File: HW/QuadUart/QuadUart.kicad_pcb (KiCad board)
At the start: 2 copper layers, 80.3 x 48.7 mm, 93 parts, among them J1 USB_C_Receptacle_USB2.0, J2 Conn_02x05_Odd_Even, J3 Conn_02x10_Odd_Even, Q1 BC847, Q2 BC847, SW1 SW_DIP_x04, SW2 SW_DIP_x01, SW3 SW_DIP_x01, U1 LN1134-3.3V, U10 SN74LV4T125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

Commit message: Finished layout, added Gerbers
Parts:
- removed C7, C8: 27pF, Capacitor_SMD:C_0603_1608Metric_Pad1.08x0.95mm_HandSolder
- added D11: LED, LED_SMD:LED_0603_1608Metric_Pad1.05x0.95mm_HandSolder, F.Cu at (170.7, 84.2)
- added J4: Conn_01x05, Connector_PinHeader_2.54mm:PinHeader_1x05_P2.54mm_Vertical, F.Cu at (192.9, 63.0)
- added LOGO1: Logo_Open_Hardware_Small, Symbol:OSHW-Logo_7.5x8mm_SilkScreen, F.Cu at (188.3, 70.2)
- added MARK1: LOGO, Kicad_Library:FOX_LOGO_MASK, B.Cu at (185.7, 86.6)
- added MARK2: LOGO, Kicad_Library:FOX_LOGO_SILK, F.Cu at (185.7, 86.6)
- added R31: 0R, Resistor_SMD:R_0603_1608Metric_Pad0.98x0.95mm_HandSolder, F.Cu at (169.2, 77.8)
- added R32: R, Resistor_SMD:R_0603_1608Metric_Pad0.98x0.95mm_HandSolder, F.Cu at (167.3, 84.2)
- Y1: value Crystal_GND24 -> Crystal_GND2; footprint Crystal:Crystal_SMD_3225-4Pin_3.2x2.5mm -> Crystal:Resonator_SMD_muRata_CSTxExxV-3Pin_3.0x1.1mm
- moved R2 10.6 mm to (158.5, 69.0), turned to 90 degrees
- moved C13 8.60 mm to (166.3, 53.1), turned to 270 degrees
- moved R24 7.23 mm to (164.8, 53.1), turned to 270 degrees
- moved R4 2.98 mm to (167.8, 87.0), turned to 180 degrees
- moved R1 2.72 mm to (158.5, 79.8), turned to 270 degrees
- moved FB2 2.46 mm to (161.2, 64.4), turned to 180 degrees
- moved C18 1.35 mm to (168.1, 73.0), turned to 180 degrees
- moved R27 1.34 mm to (205.1, 80.8), turned to 270 degrees
- moved R29 1.27 mm to (206.9, 67.9), turned to 90 degrees
- moved R3 1.26 mm to (164.0, 87.0), turned to 0 degrees
- moved R30 1.15 mm to (205.1, 67.9), turned to 90 degrees
- moved R28 1.10 mm to (206.9, 80.8), turned to 270 degrees
- moved R19 1.04 mm to (167.9, 53.1), turned to 270 degrees
- moved FB1 0.97 mm to (161.2, 66.3)
- moved R20 0.64 mm to (166.9, 63.1)
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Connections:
- C15 pad 1: VCC -> +3V3
- C17 pad 1: +3V3 -> VCC
- R14 pad 2: VCC -> /PWR_1
- R16 pad 2: VDD -> /PWR_2
- SW2 pad 1: Net-(C11-Pad1) -> VDD
- SW2 pad 2: VDD -> Net-(C11-Pad1)
- SW3 pad 1: Net-(C11-Pad1) -> VCC
- SW3 pad 2: VCC -> Net-(C11-Pad1)
- U10 pad 11: /DTR_2_UC -> /RX_3_RES
- U10 pad 12: /DTR_2_RES -> /RX_3_UC
- U10 pad 14: VCC -> +3V3
- U10 pad 2: /TX_1_UC -> /RX_2_RES
- U10 pad 3: /TX_1_RES -> /RX_2_UC
- U10 pad 5: /TX_2_UC -> /RX_1_RES
- U10 pad 6: /TX_2_RES -> /RX_1_UC
- U10 pad 8: /DTR_1_RES -> /RX_4_UC
- U10 pad 9: /DTR_1_UC -> /RX_4_RES
- U11 pad 2: /TX_3_UC -> /TX_4_UC
- U11 pad 3: /TX_3_RES -> /TX_4_RES
- U11 pad 5: /TX_4_UC -> /TX_3_UC
- U11 pad 6: /TX_4_RES -> /TX_3_RES
- U2 pad 1: /TX_2_RES -> /RX_2_RES
- U2 pad 3: /TX_1_RES -> /RX_1_RES
- U2 pad 4: /RX_2_RES -> /TX_2_RES
- U2 pad 6: /RX_1_RES -> /TX_1_RES
- U3 pad 1: /TX_4_RES -> Net-(U3-Pad1)
- U3 pad 3: /TX_3_RES -> Net-(U3-Pad3)
- U3 pad 4: /RX_4_RES -> /TX_4_RES
- U3 pad 6: /RX_3_RES -> /TX_3_RES
- U4 pad 1: /D- -> /D+
- U4 pad 3: /D- -> Net-(U4-Pad3)
- U4 pad 4: /D+ -> Net-(U4-Pad4)
- U4 pad 6: /D+ -> /D-
- U6 pad 4: Net-(U6-Pad4) -> /RX_4_RES
- U6 pad 6: Net-(U6-Pad6) -> /RX_3_RES
- U7 pad 1: /LED_RX_3 -> /LED_TX_2
- U7 pad 11: Net-(U7-Pad11) -> /DTR_3_UC
- U7 pad 12: Net-(U7-Pad12) -> /DTR_4_UC
- U7 pad 13: Net-(U7-Pad13) -> /LED_TX_3
- U7 pad 14: Net-(U7-Pad14) -> /LED_RX_3
- U7 pad 15: Net-(U7-Pad15) -> /LED_TX_4
- U7 pad 16: Net-(U7-Pad16) -> /LED_RX_4
- U7 pad 17: Net-(U7-Pad17) -> /PGEC2
- U7 pad 18: Net-(U7-Pad18) -> /PGED2
- U7 pad 2: /LED_TX_4 -> /LED_RX_1
- U7 pad 21: Net-(U7-Pad21) -> /RX_4_UC
- U7 pad 29: Net-(U7-Pad29) -> /TX_4_UC
- U7 pad 3: /LED_RX_4 -> /LED_TX_1
- U7 pad 31: /RX_2_UC -> /RX_3_UC
- U7 pad 32: /TX_2_UC -> /TX_3_UC
- U7 pad 4: /TX_DBG -> /TX_2_UC
- U7 pad 43: /RX_4_UC -> Net-(U7-Pad43)
- U7 pad 49: /TX_4_UC -> Net-(U7-Pad49)
- U7 pad 5: /RX_3_UC -> /RX_1_UC
- U7 pad 50: /RX_1_UC -> /RX_DBG
- U7 pad 51: /TX_1_UC -> /TX_DBG
- U7 pad 54: /DTR_3_UC -> Net-(U7-Pad54)
- U7 pad 55: /DTR_4_UC -> Net-(U7-Pad55)
- U7 pad 6: /TX_3_UC -> /TX_1_UC
- U7 pad 60: /LED_TX_1 -> Net-(U7-Pad60)
- U7 pad 61: /LED_RX_1 -> Net-(U7-Pad61)
- U7 pad 62: /LED_TX_2 -> Net-(U7-Pad62)
- U7 pad 63: /LED_RX_2 -> Net-(U7-Pad63)
- U7 pad 64: /LED_TX_3 -> /LED_RX_2
- U7 pad 8: /RX_DBG -> /RX_2_UC
- U9 pad 11: /RX_4_RES -> /DTR_1_UC
- U9 pad 12: /RX_4_UC -> /DTR_1_RES
- U9 pad 14: +3V3 -> VCC
- U9 pad 2: /RX_1_RES -> /TX_2_UC
- U9 pad 3: /RX_1_UC -> /TX_2_RES
- U9 pad 5: /RX_2_RES -> /TX_1_UC
- U9 pad 6: /RX_2_UC -> /TX_1_RES
- U9 pad 8: /RX_3_UC -> /DTR_2_RES
- U9 pad 9: /RX_3_RES -> /DTR_2_UC
- Y1 pad 3: /OSC2 -> Net-(R31-Pad1)
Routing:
- net +3V3: track 0.00 -> 175.5 mm, vias 0 -> 4
- net Net-(C11-Pad1): track 0.00 -> 121.7 mm, vias 0 -> 2
- net /~MCLR~: track 0.00 -> 60.3 mm, vias 0 -> 4
- net /PWR_2: track 0.00 -> 50.5 mm, vias 0 -> 6
- net /PWR_1: track 0.00 -> 43.4 mm, vias 0 -> 2
- net VCC: track 0.00 -> 43.2 mm, vias 0 -> 1
- net VDD: track 0.00 -> 38.9 mm, vias 0 -> 3
- net /TDI: track 0.00 -> 35.9 mm
- net /TDO: track 0.00 -> 35.3 mm
- net /TX_3_UC: track 0.00 -> 34.7 mm, vias 0 -> 2
- net /TCK: track 0.00 -> 33.6 mm
- net /LED_TX_3: track 0.00 -> 33.0 mm
- net /DTR_1_UC: track 0.00 -> 31.6 mm, vias 0 -> 2
- net /TMS: track 0.00 -> 31.5 mm, vias 0 -> 2
- net /DTR_2_UC: track 0.00 -> 31.0 mm, vias 0 -> 2
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- added copper zone on F.Cu, net Net-(L1-Pad1)
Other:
- rule via_min_size: 0.4 -> 0.6
- board text added: "+"
- board text added: "Bank 1"
- board text added: "Bank 2"
- board text added: "D"
- board text added: "DTR"
- board text added: "DTR + 2 GND RX TX DTR + 1 GND RX TX"
- board text added: "GND"
- board text added: "QuadUart (PIC32MX)"
- board text added: "QuadUart, TX/RX/GND/VCC/DTR 2 Banks (2x2 UARTs) /w Power supply 1.8-5.5V"
- board text added: "RX"
- board text added: "TX"

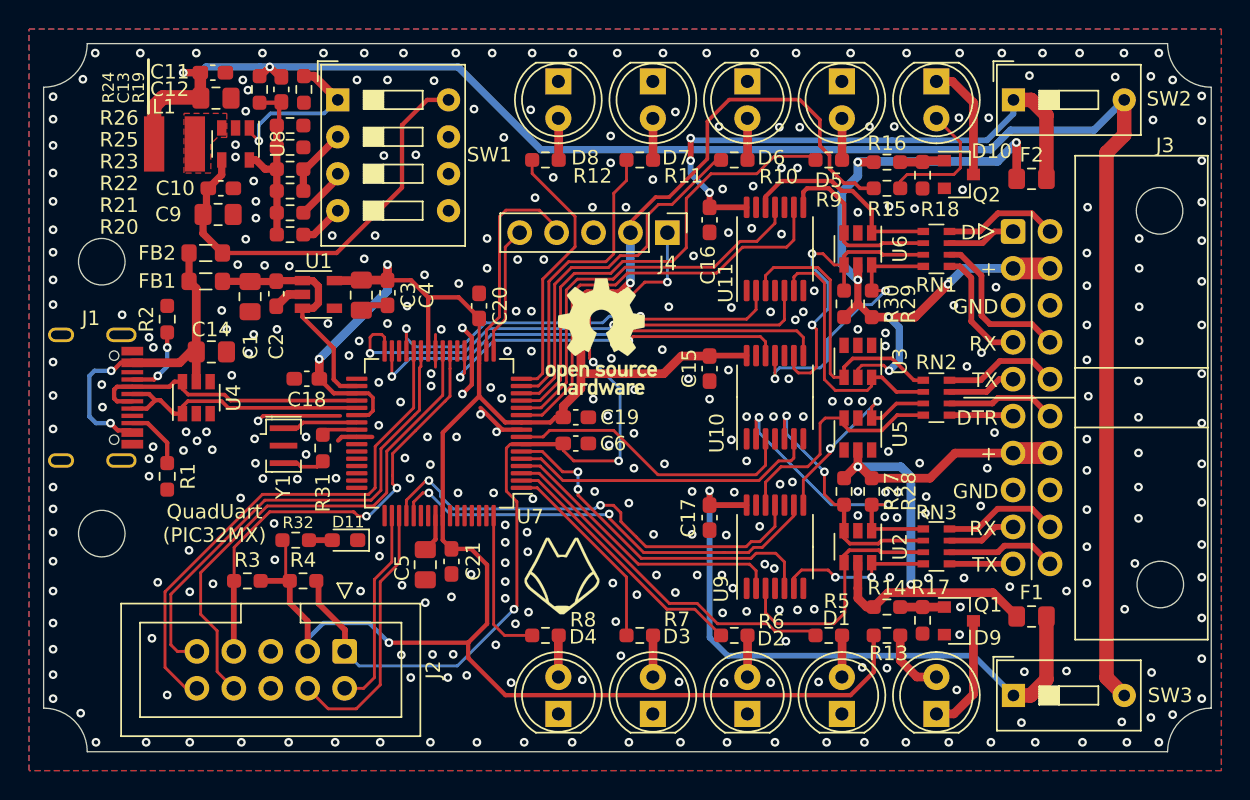
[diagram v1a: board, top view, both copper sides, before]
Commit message: Added 2 capacitors (ESD) and changed fuse position.
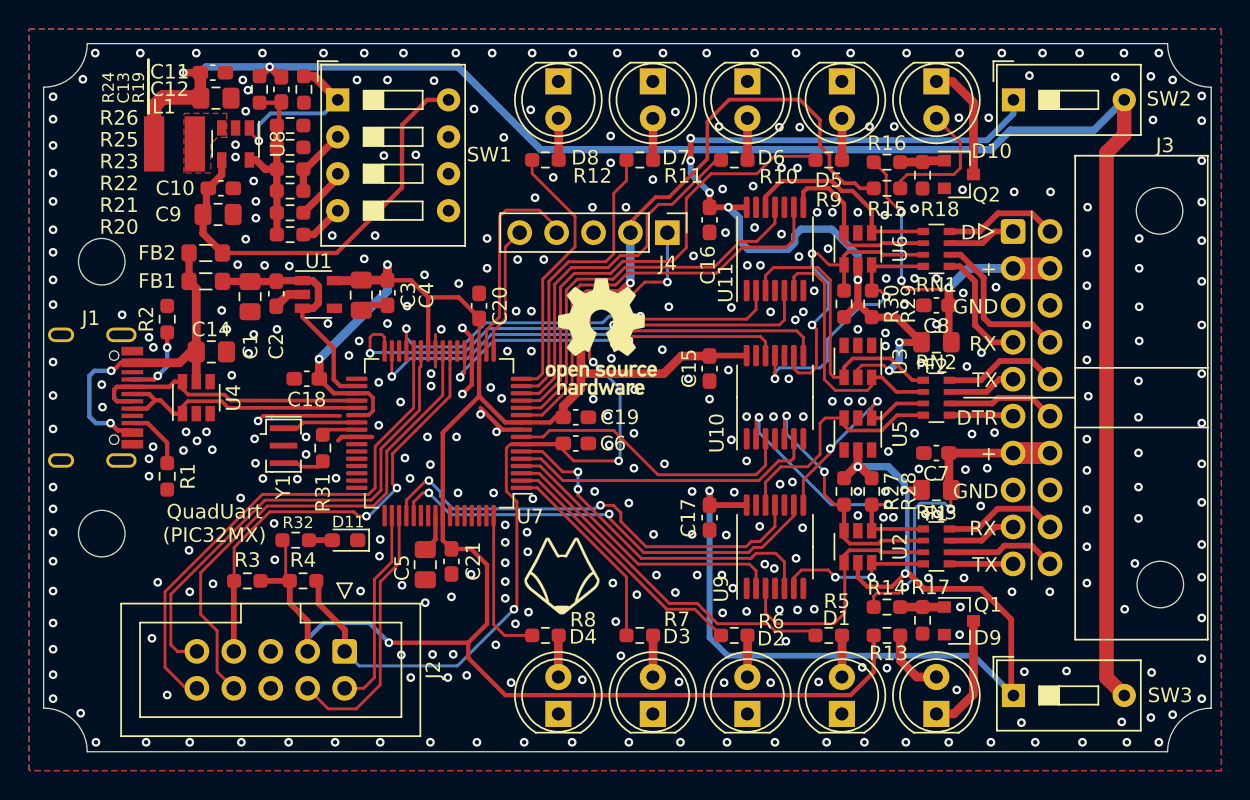
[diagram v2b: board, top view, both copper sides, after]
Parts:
- added C7: 100nF, Capacitor_SMD:C_0603_1608Metric_Pad1.08x0.95mm_HandSolder, F.Cu at (211.4, 78.2)
- added C8: 100nF, Capacitor_SMD:C_0603_1608Metric_Pad1.08x0.95mm_HandSolder, F.Cu at (211.4, 68.0)
- moved F2 13.0 mm to (211.4, 70.5), turned to 180 degrees
- moved F1 10.9 mm to (211.4, 80.7), turned to 180 degrees
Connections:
- R27 pad 1: /PWR_1 -> VCC
- R28 pad 1: /PWR_1 -> VCC
- R29 pad 1: /PWR_2 -> VDD
- R30 pad 1: /PWR_2 -> VDD
- U2 pad 5: /PWR_1 -> VCC
- U3 pad 5: /PWR_2 -> VDD
- U5 pad 5: /PWR_1 -> VCC
- U6 pad 5: /PWR_2 -> VDD
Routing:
- net VCC: track 43.2 -> 69.9 mm, vias 1 -> 4
- net /PWR_2: track 50.5 -> 23.9 mm, vias 6 -> 3
- net VDD: track 38.9 -> 62.6 mm, vias 3 -> 7
- net /PWR_1: track 43.4 -> 22.6 mm
- net GND: vias 355 -> 372
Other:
- board text added: "QuadUart TX/RX/GND/VCC/DTR 2 Banks (2x2 UARTs) /w Power supply 1.8-5.5V"
- board text removed: "QuadUart, TX/RX/GND/VCC/DTR 2 Banks (2x2 UARTs) /w Power supply 1.8-5.5V"

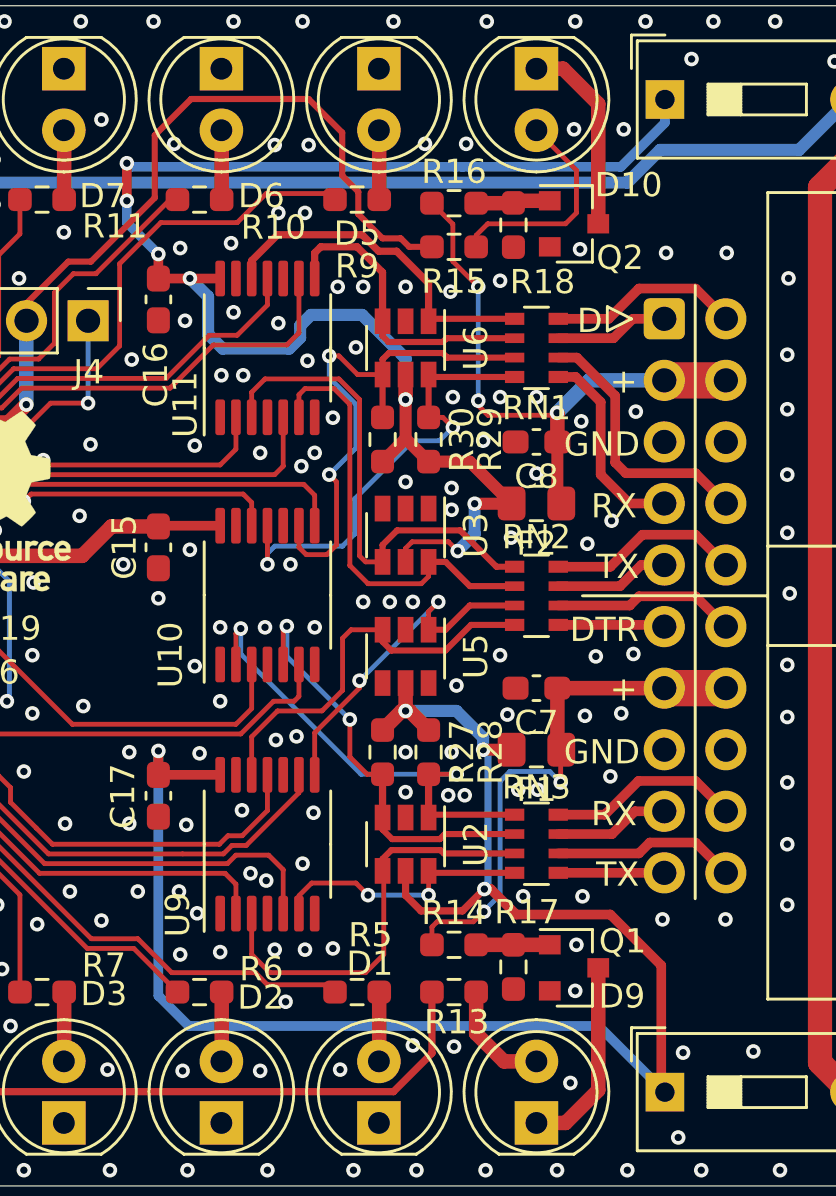
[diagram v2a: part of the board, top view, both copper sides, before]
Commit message: Modified silkscreen. Exported gerbers
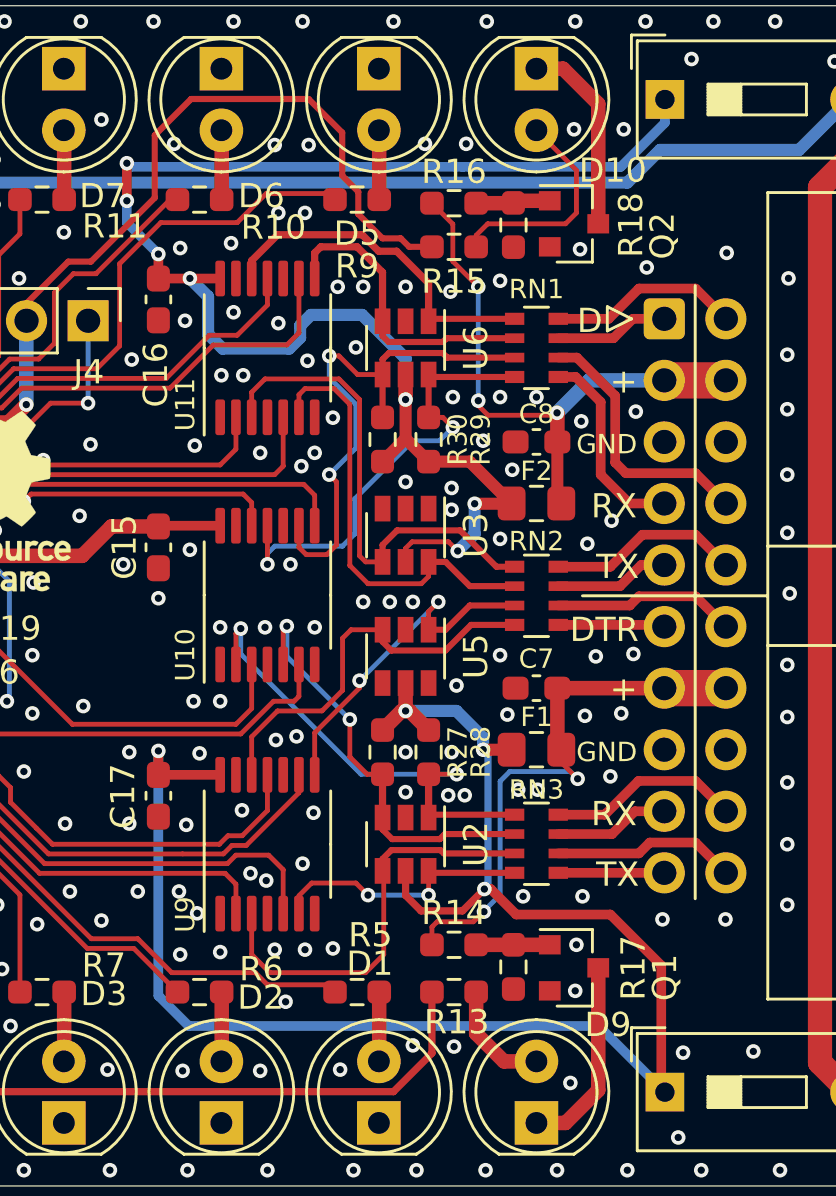
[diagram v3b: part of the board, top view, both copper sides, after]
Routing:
- net /PWR_1: track 22.6 -> 23.3 mm
